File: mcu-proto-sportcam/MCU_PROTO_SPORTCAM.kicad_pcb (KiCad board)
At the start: 2 copper layers, 59 x 41 mm, 256 parts, among them J3 Conn_01x08_Female, J4 Conn_01x08_Female, J5 Conn_01x08_Female, J6 Conn_01x08_Female, J7 Conn_01x01_Male, J8 Conn_01x01_Male

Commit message: mcu proto sportcam deleted previous items
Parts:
- removed J3, J4, J5, J6: Conn_01x08_Female, Connector_PinSocket_2.54mm:PinSocket_1x08_P2.54mm_Vertical
- removed J7, J8: Conn_01x01_Male, Connector_Wire:SolderWirePad_1x01_Drill0.8mm
- removed the REF** at (122.2, 133.4)
- removed the REF** at (119.6, 133.4)
- removed the REF** at (117.1, 133.4)
- removed the REF** at (114.5, 133.4)
- removed the REF** at (112.0, 133.4)
- removed the REF** at (127.2, 115.6)
- removed the REF** at (124.7, 115.6)
- removed the REF** at (122.2, 115.6)
- removed the REF** at (119.6, 115.6)
- removed the REF** at (117.1, 115.6)
- removed the REF** at (114.5, 115.6)
- removed the REF** at (112.0, 115.6)
- removed the REF** at (127.2, 110.5)
- removed the REF** at (124.7, 110.5)
- removed the REF** at (122.2, 110.5)
- removed the REF** at (119.6, 110.5)
- removed the REF** at (117.1, 110.5)
- removed the REF** at (114.5, 110.5)
- removed the REF** at (112.0, 110.5)
- removed the REF** at (124.7, 118.2)
- removed the REF** at (124.7, 120.7)
- removed the REF** at (124.7, 123.2)
- removed the REF** at (124.7, 125.8)
- removed the REF** at (124.7, 128.3)
- removed the REF** at (124.7, 130.9)
- removed the REF** at (106.9, 118.2)
- removed the REF** at (106.9, 120.7)
- removed the REF** at (106.9, 123.2)
- removed the REF** at (106.9, 125.8)
- removed the REF** at (106.9, 128.3)
- removed the REF** at (106.9, 130.9)
- removed the REF** at (106.9, 133.4)
- removed the REF** at (101.8, 118.2)
- removed the REF** at (101.8, 120.7)
- removed the REF** at (101.8, 123.2)
- removed the REF** at (101.8, 125.8)
- removed the REF** at (101.8, 128.3)
- removed the REF** at (101.8, 130.9)
- removed the REF** at (101.8, 133.4)
- removed the REF** at (101.8, 135.9)
- removed the REF** at (109.5, 115.6)
- removed the REF** at (109.5, 110.5)
- removed the REF** at (106.9, 135.9)
- removed the REF** at (124.7, 133.4)
- removed the REF** at (109.5, 133.4)
- removed the REF** at (115.7, 127.3)
- removed the REF** at (115.9, 127.1)
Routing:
- net (no net): track 772.8 -> 757.6 mm
- net Net-(J4-Pad7): track 9.29 -> 0.00 mm
- net Net-(J4-Pad8): track 9.09 -> 0.00 mm
- net Net-(J5-Pad3): track 8.05 -> 0.00 mm
- net Net-(J5-Pad1): track 8.04 -> 0.00 mm
- net Net-(J6-Pad6): track 7.64 -> 0.00 mm
- net Net-(J5-Pad4): track 7.62 -> 0.00 mm
- net Net-(J6-Pad2): track 7.55 -> 0.00 mm
- net Net-(J6-Pad3): track 7.49 -> 0.00 mm
- net Net-(J5-Pad6): track 7.45 -> 0.00 mm
- net Net-(J4-Pad1): track 7.44 -> 0.00 mm
- net Net-(J3-Pad2): track 7.28 -> 0.00 mm
- net Net-(J3-Pad6): track 7.18 -> 0.00 mm
- net Net-(J5-Pad5): track 7.09 -> 0.00 mm
- net Net-(J6-Pad4): track 7.06 -> 0.00 mm
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- added copper zone on B.Cu, net (none)
- added copper zone on F.Cu, net (none)
- removed copper zone on B.Cu, net Net-(J7-Pad1)
- removed copper zone on F.Cu, net Net-(J7-Pad1)
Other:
- board text added: "MCU PROTO SPORTCAM"
- board text removed: "ESP32CAM PROTO SPORTCAM"

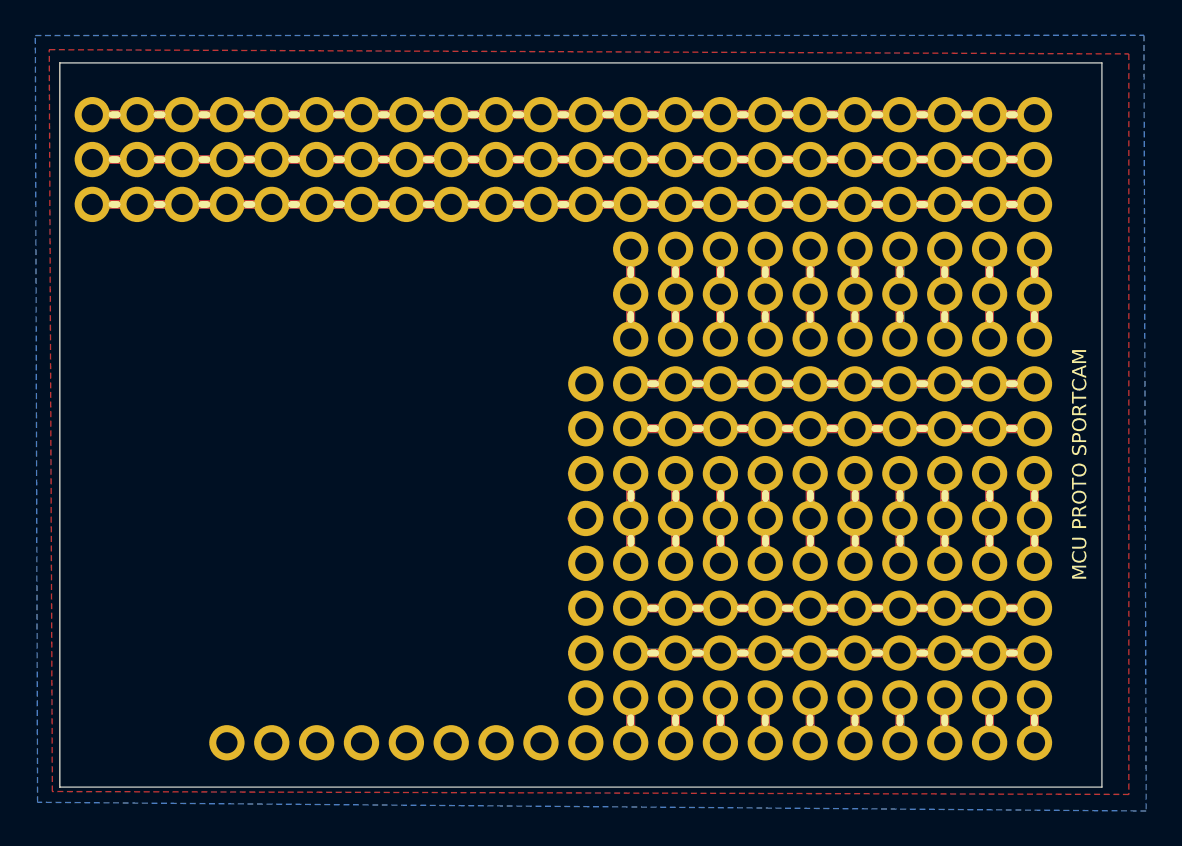
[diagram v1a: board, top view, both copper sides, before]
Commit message: mcu proto sportcam deleted previous tracks
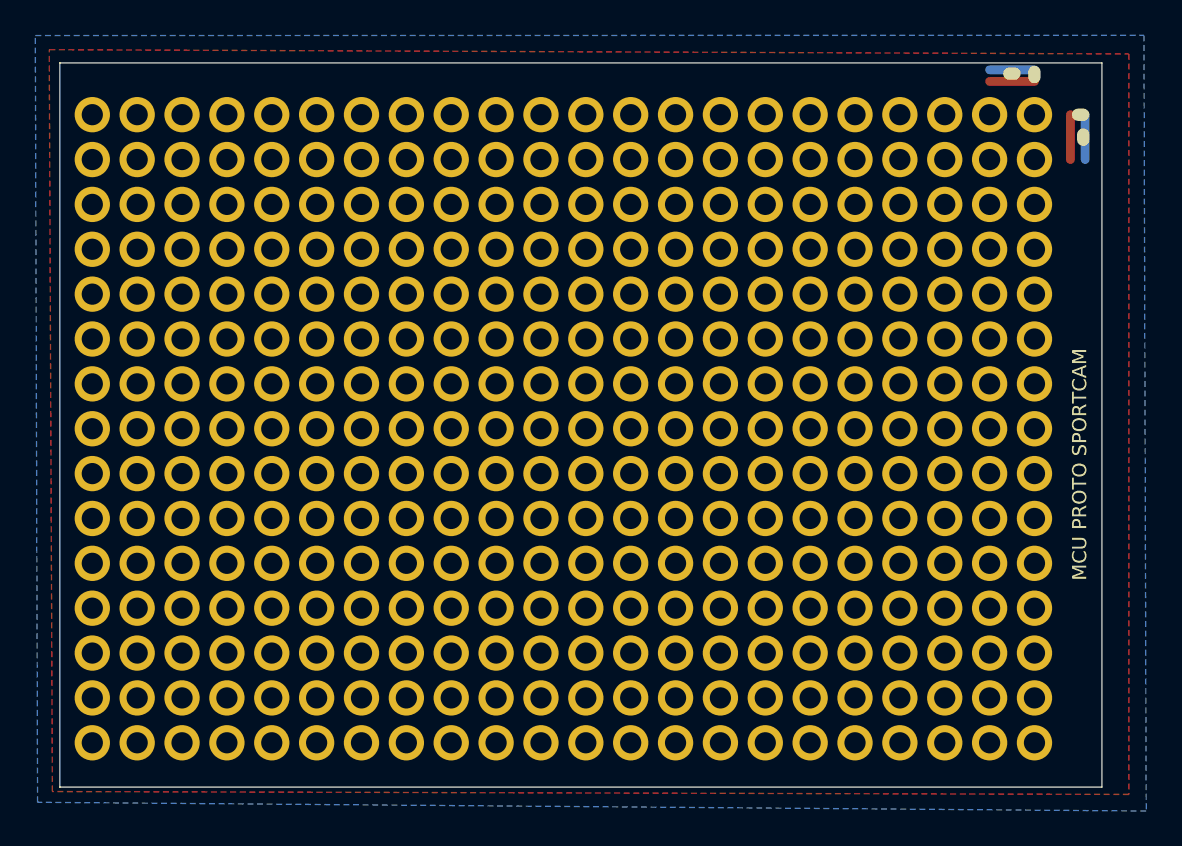
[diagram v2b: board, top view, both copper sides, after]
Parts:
- added REF**: SolderWirePad_1x01_Drill0.8mm, Connector_Wire:SolderWirePad_1x01_Drill0.8mm, F.Cu at (127.2, 135.9)
- added REF**: SolderWirePad_1x01_Drill0.8mm, Connector_Wire:SolderWirePad_1x01_Drill0.8mm, F.Cu at (104.4, 135.9)
- added REF**: SolderWirePad_1x01_Drill0.8mm, Connector_Wire:SolderWirePad_1x01_Drill0.8mm, F.Cu at (109.5, 115.6)
- added REF**: SolderWirePad_1x01_Drill0.8mm, Connector_Wire:SolderWirePad_1x01_Drill0.8mm, F.Cu at (106.9, 115.6)
- added REF**: SolderWirePad_1x01_Drill0.8mm, Connector_Wire:SolderWirePad_1x01_Drill0.8mm, F.Cu at (104.4, 115.6)
- added REF**: SolderWirePad_1x01_Drill0.8mm, Connector_Wire:SolderWirePad_1x01_Drill0.8mm, F.Cu at (101.8, 115.6)
- added REF**: SolderWirePad_1x01_Drill0.8mm, Connector_Wire:SolderWirePad_1x01_Drill0.8mm, F.Cu at (129.8, 113.1)
- added REF**: SolderWirePad_1x01_Drill0.8mm, Connector_Wire:SolderWirePad_1x01_Drill0.8mm, F.Cu at (127.2, 113.1)
- added REF**: SolderWirePad_1x01_Drill0.8mm, Connector_Wire:SolderWirePad_1x01_Drill0.8mm, F.Cu at (124.7, 113.1)
- added REF**: SolderWirePad_1x01_Drill0.8mm, Connector_Wire:SolderWirePad_1x01_Drill0.8mm, F.Cu at (122.2, 113.1)
- added REF**: SolderWirePad_1x01_Drill0.8mm, Connector_Wire:SolderWirePad_1x01_Drill0.8mm, F.Cu at (119.6, 113.1)
- added REF**: SolderWirePad_1x01_Drill0.8mm, Connector_Wire:SolderWirePad_1x01_Drill0.8mm, F.Cu at (117.1, 113.1)
- added REF**: SolderWirePad_1x01_Drill0.8mm, Connector_Wire:SolderWirePad_1x01_Drill0.8mm, F.Cu at (101.8, 135.9)
- added REF**: SolderWirePad_1x01_Drill0.8mm, Connector_Wire:SolderWirePad_1x01_Drill0.8mm, F.Cu at (114.5, 113.1)
- added REF**: SolderWirePad_1x01_Drill0.8mm, Connector_Wire:SolderWirePad_1x01_Drill0.8mm, F.Cu at (112.0, 113.1)
- added REF**: SolderWirePad_1x01_Drill0.8mm, Connector_Wire:SolderWirePad_1x01_Drill0.8mm, F.Cu at (109.5, 113.1)
- added REF**: SolderWirePad_1x01_Drill0.8mm, Connector_Wire:SolderWirePad_1x01_Drill0.8mm, F.Cu at (106.9, 113.1)
- added REF**: SolderWirePad_1x01_Drill0.8mm, Connector_Wire:SolderWirePad_1x01_Drill0.8mm, F.Cu at (104.4, 113.1)
- added REF**: SolderWirePad_1x01_Drill0.8mm, Connector_Wire:SolderWirePad_1x01_Drill0.8mm, F.Cu at (101.8, 113.1)
- added REF**: SolderWirePad_1x01_Drill0.8mm, Connector_Wire:SolderWirePad_1x01_Drill0.8mm, F.Cu at (129.8, 110.5)
- added REF**: SolderWirePad_1x01_Drill0.8mm, Connector_Wire:SolderWirePad_1x01_Drill0.8mm, F.Cu at (127.2, 110.5)
- added REF**: SolderWirePad_1x01_Drill0.8mm, Connector_Wire:SolderWirePad_1x01_Drill0.8mm, F.Cu at (124.7, 110.5)
- added REF**: SolderWirePad_1x01_Drill0.8mm, Connector_Wire:SolderWirePad_1x01_Drill0.8mm, F.Cu at (122.2, 110.5)
- added REF**: SolderWirePad_1x01_Drill0.8mm, Connector_Wire:SolderWirePad_1x01_Drill0.8mm, F.Cu at (127.2, 133.4)
- added REF**: SolderWirePad_1x01_Drill0.8mm, Connector_Wire:SolderWirePad_1x01_Drill0.8mm, F.Cu at (119.6, 110.5)
- added REF**: SolderWirePad_1x01_Drill0.8mm, Connector_Wire:SolderWirePad_1x01_Drill0.8mm, F.Cu at (117.1, 110.5)
- added REF**: SolderWirePad_1x01_Drill0.8mm, Connector_Wire:SolderWirePad_1x01_Drill0.8mm, F.Cu at (114.5, 110.5)
- added REF**: SolderWirePad_1x01_Drill0.8mm, Connector_Wire:SolderWirePad_1x01_Drill0.8mm, F.Cu at (112.0, 110.5)
- added REF**: SolderWirePad_1x01_Drill0.8mm, Connector_Wire:SolderWirePad_1x01_Drill0.8mm, F.Cu at (109.5, 110.5)
- added REF**: SolderWirePad_1x01_Drill0.8mm, Connector_Wire:SolderWirePad_1x01_Drill0.8mm, F.Cu at (106.9, 110.5)
- added REF**: SolderWirePad_1x01_Drill0.8mm, Connector_Wire:SolderWirePad_1x01_Drill0.8mm, F.Cu at (104.4, 110.5)
- added REF**: SolderWirePad_1x01_Drill0.8mm, Connector_Wire:SolderWirePad_1x01_Drill0.8mm, F.Cu at (101.8, 110.5)
- added REF**: SolderWirePad_1x01_Drill0.8mm, Connector_Wire:SolderWirePad_1x01_Drill0.8mm, F.Cu at (124.7, 133.4)
- added REF**: SolderWirePad_1x01_Drill0.8mm, Connector_Wire:SolderWirePad_1x01_Drill0.8mm, F.Cu at (122.2, 133.4)
- added REF**: SolderWirePad_1x01_Drill0.8mm, Connector_Wire:SolderWirePad_1x01_Drill0.8mm, F.Cu at (119.6, 133.4)
- added REF**: SolderWirePad_1x01_Drill0.8mm, Connector_Wire:SolderWirePad_1x01_Drill0.8mm, F.Cu at (117.1, 133.4)
- added REF**: SolderWirePad_1x01_Drill0.8mm, Connector_Wire:SolderWirePad_1x01_Drill0.8mm, F.Cu at (114.5, 133.4)
- added REF**: SolderWirePad_1x01_Drill0.8mm, Connector_Wire:SolderWirePad_1x01_Drill0.8mm, F.Cu at (112.0, 133.4)
- added REF**: SolderWirePad_1x01_Drill0.8mm, Connector_Wire:SolderWirePad_1x01_Drill0.8mm, F.Cu at (109.5, 133.4)
- added REF**: SolderWirePad_1x01_Drill0.8mm, Connector_Wire:SolderWirePad_1x01_Drill0.8mm, F.Cu at (124.7, 135.9)
- added REF**: SolderWirePad_1x01_Drill0.8mm, Connector_Wire:SolderWirePad_1x01_Drill0.8mm, F.Cu at (106.9, 133.4)
- added REF**: SolderWirePad_1x01_Drill0.8mm, Connector_Wire:SolderWirePad_1x01_Drill0.8mm, F.Cu at (104.4, 133.4)
- added REF**: SolderWirePad_1x01_Drill0.8mm, Connector_Wire:SolderWirePad_1x01_Drill0.8mm, F.Cu at (101.8, 133.4)
- added REF**: SolderWirePad_1x01_Drill0.8mm, Connector_Wire:SolderWirePad_1x01_Drill0.8mm, F.Cu at (127.2, 130.9)
- added REF**: SolderWirePad_1x01_Drill0.8mm, Connector_Wire:SolderWirePad_1x01_Drill0.8mm, F.Cu at (124.7, 130.9)
- added REF**: SolderWirePad_1x01_Drill0.8mm, Connector_Wire:SolderWirePad_1x01_Drill0.8mm, F.Cu at (122.2, 130.9)
- added REF**: SolderWirePad_1x01_Drill0.8mm, Connector_Wire:SolderWirePad_1x01_Drill0.8mm, F.Cu at (119.6, 130.9)
- added REF**: SolderWirePad_1x01_Drill0.8mm, Connector_Wire:SolderWirePad_1x01_Drill0.8mm, F.Cu at (117.1, 130.9)
- added REF**: SolderWirePad_1x01_Drill0.8mm, Connector_Wire:SolderWirePad_1x01_Drill0.8mm, F.Cu at (114.5, 130.9)
- added REF**: SolderWirePad_1x01_Drill0.8mm, Connector_Wire:SolderWirePad_1x01_Drill0.8mm, F.Cu at (112.0, 130.9)
- added REF**: SolderWirePad_1x01_Drill0.8mm, Connector_Wire:SolderWirePad_1x01_Drill0.8mm, F.Cu at (122.2, 135.9)
- added REF**: SolderWirePad_1x01_Drill0.8mm, Connector_Wire:SolderWirePad_1x01_Drill0.8mm, F.Cu at (109.5, 130.9)
- added REF**: SolderWirePad_1x01_Drill0.8mm, Connector_Wire:SolderWirePad_1x01_Drill0.8mm, F.Cu at (106.9, 130.9)
- added REF**: SolderWirePad_1x01_Drill0.8mm, Connector_Wire:SolderWirePad_1x01_Drill0.8mm, F.Cu at (104.4, 130.9)
- added REF**: SolderWirePad_1x01_Drill0.8mm, Connector_Wire:SolderWirePad_1x01_Drill0.8mm, F.Cu at (101.8, 130.9)
- added REF**: SolderWirePad_1x01_Drill0.8mm, Connector_Wire:SolderWirePad_1x01_Drill0.8mm, F.Cu at (127.2, 128.3)
- added REF**: SolderWirePad_1x01_Drill0.8mm, Connector_Wire:SolderWirePad_1x01_Drill0.8mm, F.Cu at (124.7, 128.3)
- added REF**: SolderWirePad_1x01_Drill0.8mm, Connector_Wire:SolderWirePad_1x01_Drill0.8mm, F.Cu at (122.2, 128.3)
- added REF**: SolderWirePad_1x01_Drill0.8mm, Connector_Wire:SolderWirePad_1x01_Drill0.8mm, F.Cu at (119.6, 128.3)
- added REF**: SolderWirePad_1x01_Drill0.8mm, Connector_Wire:SolderWirePad_1x01_Drill0.8mm, F.Cu at (117.1, 128.3)
- added REF**: SolderWirePad_1x01_Drill0.8mm, Connector_Wire:SolderWirePad_1x01_Drill0.8mm, F.Cu at (114.5, 128.3)
- added REF**: SolderWirePad_1x01_Drill0.8mm, Connector_Wire:SolderWirePad_1x01_Drill0.8mm, F.Cu at (119.6, 135.9)
- added REF**: SolderWirePad_1x01_Drill0.8mm, Connector_Wire:SolderWirePad_1x01_Drill0.8mm, F.Cu at (112.0, 128.3)
- added REF**: SolderWirePad_1x01_Drill0.8mm, Connector_Wire:SolderWirePad_1x01_Drill0.8mm, F.Cu at (109.5, 128.3)
- added REF**: SolderWirePad_1x01_Drill0.8mm, Connector_Wire:SolderWirePad_1x01_Drill0.8mm, F.Cu at (106.9, 128.3)
- added REF**: SolderWirePad_1x01_Drill0.8mm, Connector_Wire:SolderWirePad_1x01_Drill0.8mm, F.Cu at (104.4, 128.3)
- added REF**: SolderWirePad_1x01_Drill0.8mm, Connector_Wire:SolderWirePad_1x01_Drill0.8mm, F.Cu at (101.8, 128.3)
- added REF**: SolderWirePad_1x01_Drill0.8mm, Connector_Wire:SolderWirePad_1x01_Drill0.8mm, F.Cu at (127.2, 125.8)
- added REF**: SolderWirePad_1x01_Drill0.8mm, Connector_Wire:SolderWirePad_1x01_Drill0.8mm, F.Cu at (124.7, 125.8)
- added REF**: SolderWirePad_1x01_Drill0.8mm, Connector_Wire:SolderWirePad_1x01_Drill0.8mm, F.Cu at (122.2, 125.8)
- added REF**: SolderWirePad_1x01_Drill0.8mm, Connector_Wire:SolderWirePad_1x01_Drill0.8mm, F.Cu at (119.6, 125.8)
- added REF**: SolderWirePad_1x01_Drill0.8mm, Connector_Wire:SolderWirePad_1x01_Drill0.8mm, F.Cu at (117.1, 125.8)
- added REF**: SolderWirePad_1x01_Drill0.8mm, Connector_Wire:SolderWirePad_1x01_Drill0.8mm, F.Cu at (117.1, 135.9)
- added REF**: SolderWirePad_1x01_Drill0.8mm, Connector_Wire:SolderWirePad_1x01_Drill0.8mm, F.Cu at (114.5, 125.8)
- added REF**: SolderWirePad_1x01_Drill0.8mm, Connector_Wire:SolderWirePad_1x01_Drill0.8mm, F.Cu at (112.0, 125.8)
- added REF**: SolderWirePad_1x01_Drill0.8mm, Connector_Wire:SolderWirePad_1x01_Drill0.8mm, F.Cu at (109.5, 125.8)
- added REF**: SolderWirePad_1x01_Drill0.8mm, Connector_Wire:SolderWirePad_1x01_Drill0.8mm, F.Cu at (106.9, 125.8)
- added REF**: SolderWirePad_1x01_Drill0.8mm, Connector_Wire:SolderWirePad_1x01_Drill0.8mm, F.Cu at (104.4, 125.8)
- added REF**: SolderWirePad_1x01_Drill0.8mm, Connector_Wire:SolderWirePad_1x01_Drill0.8mm, F.Cu at (101.8, 125.8)
- added REF**: SolderWirePad_1x01_Drill0.8mm, Connector_Wire:SolderWirePad_1x01_Drill0.8mm, F.Cu at (127.2, 123.2)
- added REF**: SolderWirePad_1x01_Drill0.8mm, Connector_Wire:SolderWirePad_1x01_Drill0.8mm, F.Cu at (124.7, 123.2)
- added REF**: SolderWirePad_1x01_Drill0.8mm, Connector_Wire:SolderWirePad_1x01_Drill0.8mm, F.Cu at (122.2, 123.2)
- added REF**: SolderWirePad_1x01_Drill0.8mm, Connector_Wire:SolderWirePad_1x01_Drill0.8mm, F.Cu at (119.6, 123.2)
- added REF**: SolderWirePad_1x01_Drill0.8mm, Connector_Wire:SolderWirePad_1x01_Drill0.8mm, F.Cu at (114.5, 135.9)
- added REF**: SolderWirePad_1x01_Drill0.8mm, Connector_Wire:SolderWirePad_1x01_Drill0.8mm, F.Cu at (117.1, 123.2)
- added REF**: SolderWirePad_1x01_Drill0.8mm, Connector_Wire:SolderWirePad_1x01_Drill0.8mm, F.Cu at (114.5, 123.2)
- added REF**: SolderWirePad_1x01_Drill0.8mm, Connector_Wire:SolderWirePad_1x01_Drill0.8mm, F.Cu at (112.0, 123.2)
- added REF**: SolderWirePad_1x01_Drill0.8mm, Connector_Wire:SolderWirePad_1x01_Drill0.8mm, F.Cu at (109.5, 123.2)
- added REF**: SolderWirePad_1x01_Drill0.8mm, Connector_Wire:SolderWirePad_1x01_Drill0.8mm, F.Cu at (106.9, 123.2)
- added REF**: SolderWirePad_1x01_Drill0.8mm, Connector_Wire:SolderWirePad_1x01_Drill0.8mm, F.Cu at (104.4, 123.2)
- added REF**: SolderWirePad_1x01_Drill0.8mm, Connector_Wire:SolderWirePad_1x01_Drill0.8mm, F.Cu at (101.8, 123.2)
- added REF**: SolderWirePad_1x01_Drill0.8mm, Connector_Wire:SolderWirePad_1x01_Drill0.8mm, F.Cu at (127.2, 120.7)
- added REF**: SolderWirePad_1x01_Drill0.8mm, Connector_Wire:SolderWirePad_1x01_Drill0.8mm, F.Cu at (124.7, 120.7)
- added REF**: SolderWirePad_1x01_Drill0.8mm, Connector_Wire:SolderWirePad_1x01_Drill0.8mm, F.Cu at (122.2, 120.7)
- added REF**: SolderWirePad_1x01_Drill0.8mm, Connector_Wire:SolderWirePad_1x01_Drill0.8mm, F.Cu at (112.0, 135.9)
- added REF**: SolderWirePad_1x01_Drill0.8mm, Connector_Wire:SolderWirePad_1x01_Drill0.8mm, F.Cu at (119.6, 120.7)
- added REF**: SolderWirePad_1x01_Drill0.8mm, Connector_Wire:SolderWirePad_1x01_Drill0.8mm, F.Cu at (117.1, 120.7)
- added REF**: SolderWirePad_1x01_Drill0.8mm, Connector_Wire:SolderWirePad_1x01_Drill0.8mm, F.Cu at (114.5, 120.7)
- added REF**: SolderWirePad_1x01_Drill0.8mm, Connector_Wire:SolderWirePad_1x01_Drill0.8mm, F.Cu at (112.0, 120.7)
- added REF**: SolderWirePad_1x01_Drill0.8mm, Connector_Wire:SolderWirePad_1x01_Drill0.8mm, F.Cu at (109.5, 120.7)
- added REF**: SolderWirePad_1x01_Drill0.8mm, Connector_Wire:SolderWirePad_1x01_Drill0.8mm, F.Cu at (106.9, 120.7)
- added REF**: SolderWirePad_1x01_Drill0.8mm, Connector_Wire:SolderWirePad_1x01_Drill0.8mm, F.Cu at (104.4, 120.7)
- added REF**: SolderWirePad_1x01_Drill0.8mm, Connector_Wire:SolderWirePad_1x01_Drill0.8mm, F.Cu at (101.8, 120.7)
- added REF**: SolderWirePad_1x01_Drill0.8mm, Connector_Wire:SolderWirePad_1x01_Drill0.8mm, F.Cu at (127.2, 118.2)
- added REF**: SolderWirePad_1x01_Drill0.8mm, Connector_Wire:SolderWirePad_1x01_Drill0.8mm, F.Cu at (124.7, 118.2)
- added REF**: SolderWirePad_1x01_Drill0.8mm, Connector_Wire:SolderWirePad_1x01_Drill0.8mm, F.Cu at (109.5, 135.9)
- added REF**: SolderWirePad_1x01_Drill0.8mm, Connector_Wire:SolderWirePad_1x01_Drill0.8mm, F.Cu at (122.2, 118.2)
- added REF**: SolderWirePad_1x01_Drill0.8mm, Connector_Wire:SolderWirePad_1x01_Drill0.8mm, F.Cu at (119.6, 118.2)
- added REF**: SolderWirePad_1x01_Drill0.8mm, Connector_Wire:SolderWirePad_1x01_Drill0.8mm, F.Cu at (117.1, 118.2)
- added REF**: SolderWirePad_1x01_Drill0.8mm, Connector_Wire:SolderWirePad_1x01_Drill0.8mm, F.Cu at (114.5, 118.2)
- added REF**: SolderWirePad_1x01_Drill0.8mm, Connector_Wire:SolderWirePad_1x01_Drill0.8mm, F.Cu at (112.0, 118.2)
- added REF**: SolderWirePad_1x01_Drill0.8mm, Connector_Wire:SolderWirePad_1x01_Drill0.8mm, F.Cu at (109.5, 118.2)
- added REF**: SolderWirePad_1x01_Drill0.8mm, Connector_Wire:SolderWirePad_1x01_Drill0.8mm, F.Cu at (106.9, 118.2)
- added REF**: SolderWirePad_1x01_Drill0.8mm, Connector_Wire:SolderWirePad_1x01_Drill0.8mm, F.Cu at (104.4, 118.2)
- added REF**: SolderWirePad_1x01_Drill0.8mm, Connector_Wire:SolderWirePad_1x01_Drill0.8mm, F.Cu at (101.8, 118.2)
- added REF**: SolderWirePad_1x01_Drill0.8mm, Connector_Wire:SolderWirePad_1x01_Drill0.8mm, F.Cu at (106.9, 138.5)
- added REF**: SolderWirePad_1x01_Drill0.8mm, Connector_Wire:SolderWirePad_1x01_Drill0.8mm, F.Cu at (106.9, 135.9)
- added REF**: SolderWirePad_1x01_Drill0.8mm, Connector_Wire:SolderWirePad_1x01_Drill0.8mm, F.Cu at (104.4, 138.5)
- added REF**: SolderWirePad_1x01_Drill0.8mm, Connector_Wire:SolderWirePad_1x01_Drill0.8mm, F.Cu at (101.8, 138.5)
- added REF**: SolderWirePad_1x01_Drill0.8mm, Connector_Wire:SolderWirePad_1x01_Drill0.8mm, F.Cu at (129.8, 115.6)
- added REF**: SolderWirePad_1x01_Drill0.8mm, Connector_Wire:SolderWirePad_1x01_Drill0.8mm, F.Cu at (127.2, 115.6)
- added REF**: SolderWirePad_1x01_Drill0.8mm, Connector_Wire:SolderWirePad_1x01_Drill0.8mm, F.Cu at (124.7, 115.6)
- added REF**: SolderWirePad_1x01_Drill0.8mm, Connector_Wire:SolderWirePad_1x01_Drill0.8mm, F.Cu at (122.2, 115.6)
- added REF**: SolderWirePad_1x01_Drill0.8mm, Connector_Wire:SolderWirePad_1x01_Drill0.8mm, F.Cu at (119.6, 115.6)
- added REF**: SolderWirePad_1x01_Drill0.8mm, Connector_Wire:SolderWirePad_1x01_Drill0.8mm, F.Cu at (117.1, 115.6)
- added REF**: SolderWirePad_1x01_Drill0.8mm, Connector_Wire:SolderWirePad_1x01_Drill0.8mm, F.Cu at (114.5, 115.6)
- added REF**: SolderWirePad_1x01_Drill0.8mm, Connector_Wire:SolderWirePad_1x01_Drill0.8mm, F.Cu at (112.0, 115.6)
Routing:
- net (no net): track 757.6 -> 10.2 mm

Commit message: mcu proto sportcam mvp ready!
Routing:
- net (no net): track 10.2 -> 1300.5 mm

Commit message: mcu proto sportcam single gerber
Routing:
- net (no net): track 1300.5 -> 1290.3 mm
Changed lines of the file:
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@@
   (general
     (thickness 1.6)
-    (drawings 263)
-    (tracks 512)
+    (drawings 260)
+    (tracks 508)
     (zones 0)
     (modules 330)
@@
   (gr_line (start 104.3813 104.34955) (end 104.3813 104.05745) (layer F.SilkS) (width 0.7))
   (gr_line (start 101.8413 104.34955) (end 101.8413 104.05745) (layer F.SilkS) (width 0.7))
-  (gr_line (start 157.94228 104.34955) (end 157.94228 104.05745) (layer F.SilkS) (width 0.7))
-  (gr_line (start 155.17876 100.80244) (end 155.17876 100.51034) (layer F.SilkS) (width 0.7))
-  (gr_line (start 157.93974 102.9335) (end 157.64764 102.9335) (layer F.SilkS) (width 0.7))
   (gr_text "MCU PROTO SPORTCAM" (at 157.61716 123.35764 -90) (layer B.SilkS)
     (effects (font (size 0.8 0.8) (thickness 0.15)) (justify mirror))
@@
   (gr_line (start 100 141) (end 159 141) (layer Edge.Cuts) (width 0.05))
   (gr_line (start 100 100) (end 159 100) (layer Edge.Cuts) (width 0.05))
-  (segment (start 152.6413 101.04628) (end 155.1813 101.04628) (width 0.5) (layer F.Cu) (net 0))
-  (segment (start 155.1813 100.39096) (end 152.6413 100.39096) (width 0.5) (layer B.Cu) (net 0))
-  (segment (start 157.21584 105.47) (end 157.21584 102.93) (width 0.5) (layer F.Cu) (net 0))
-  (segment (start 158.04896 102.93) (end 158.04896 105.47) (width 0.5) (layer B.Cu) (net 0))
   (segment (start 101.8413 102.93) (end 101.8413 105.47) (width 0.5) (layer B.Cu) (net 0))
   (segment (start 104.3813 102.93) (end 104.3813 105.47) (width 0.5) (layer B.Cu) (net 0))
